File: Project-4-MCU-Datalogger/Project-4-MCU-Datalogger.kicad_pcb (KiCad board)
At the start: 2 copper layers, 0 parts

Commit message: update PCBNew from Schematic
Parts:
- added BT1: Battery, Connector_PinHeader_2.54mm:PinHeader_1x02_P2.54mm_Vertical, F.Cu at (208.3, 96.0)
- added C1: 0.1uF, Capacitor_SMD:C_0805_2012Metric, F.Cu at (230.6, 86.2)
- added C2: 22pF, Capacitor_SMD:C_0805_2012Metric, F.Cu at (230.6, 89.2)
- added C3: 22pF, Capacitor_SMD:C_0805_2012Metric, F.Cu at (230.6, 92.2)
- added C4: 0.1uF, Capacitor_SMD:C_0805_2012Metric, F.Cu at (230.6, 95.2)
- added C5: 100nF, Capacitor_SMD:C_0805_2012Metric, F.Cu at (230.6, 98.2)
- added D1: LED, LED_SMD:LED_0805_2012Metric, F.Cu at (235.1, 86.2)
- added D2: LED, LED_SMD:LED_0805_2012Metric, F.Cu at (235.1, 89.2)
- added H1: MountingHole, MountingHole:MountingHole_2.1mm, F.Cu at (208.9, 73.6)
- added H2: MountingHole, MountingHole:MountingHole_2.1mm, F.Cu at (208.9, 79.4)
- added H3: MountingHole, MountingHole:MountingHole_2.1mm, F.Cu at (208.9, 85.1)
- added H4: MountingHole, MountingHole:MountingHole_2.1mm, F.Cu at (208.9, 90.9)
- added J1: Conn_01x04_Pin, Connector_PinHeader_2.54mm:PinHeader_1x04_P2.54mm_Vertical, F.Cu at (246.2, 73.0)
- added J2: Conn_01x04_Pin, Connector_PinHeader_2.54mm:PinHeader_1x04_P2.54mm_Vertical, F.Cu at (250.8, 73.0)
- added J3: Conn_01x09_Pin, Connector_PinHeader_2.54mm:PinHeader_1x09_P2.54mm_Vertical, F.Cu at (241.6, 73.0)
- added J4: Conn_02x03_Odd_Even, Connector_PinHeader_2.54mm:PinHeader_2x03_P2.54mm_Vertical, F.Cu at (246.2, 85.3)
- added R1: 10K, Resistor_SMD:R_0805_2012Metric, F.Cu at (214.0, 72.2)
- added R2: 10K, Resistor_SMD:R_0805_2012Metric, F.Cu at (214.0, 75.2)
- added R3: 4.7K, Resistor_SMD:R_0805_2012Metric, F.Cu at (214.0, 78.1)
- added R4: 4.7K, Resistor_SMD:R_0805_2012Metric, F.Cu at (214.0, 81.1)
- added R5: 330, Resistor_SMD:R_0805_2012Metric, F.Cu at (214.0, 84.0)
- added R6: 10K, Resistor_SMD:R_0805_2012Metric, F.Cu at (214.0, 87.0)
- added R7: 330, Resistor_SMD:R_0805_2012Metric, F.Cu at (214.0, 89.9)
- added U1: 24LC1025, Package_SO:SOIC-8_5.3x5.3mm_P1.27mm, F.Cu at (221.3, 74.3)
- added U2: 24LC1025, Package_SO:SOIC-8_5.3x5.3mm_P1.27mm, F.Cu at (221.3, 81.2)
- added U3: DS1337S_, DS1337S_:SOIC127P600X175-8N, F.Cu at (221.3, 99.3)
- added U4: ATMEGA328P-AU, ATMEGA328P-AU:QFP80P900X900X120-32N, F.Cu at (222.7, 90.3)
- added Y1: 16 MHz, Crystal:Crystal_SMD_5032-2Pin_5.0x3.2mm_HandSoldering, F.Cu at (231.7, 73.4)
- added Y2: 32.768 KHz, Crystal:Crystal_SMD_5032-2Pin_5.0x3.2mm_HandSoldering, F.Cu at (231.7, 78.6)

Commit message: place footprints
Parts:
- moved J3 184.3 mm to (57.3, 77.8), turned to 90 degrees
- moved Y2 179.2 mm to (52.8, 69.0), turned to 90 degrees
- moved J2 167.9 mm to (82.9, 77.8), turned to 90 degrees
- moved C1 166.2 mm to (68.0, 52.0)
- moved C3 163.6 mm to (72.0, 52.0)
- moved U3 163.5 mm to (60.8, 68.2)
- moved U1 162.2 mm to (60.5, 53.5)
- moved U2 162.2 mm to (60.5, 60.5)
- moved C5 161.1 mm to (76.2, 52.2)
- moved BT1 160.0 mm to (52.8, 58.5)
- moved H1 157.8 mm to (52.5, 52.2)
- moved H3 156.5 mm to (52.5, 77.8)
- moved Y1 156.4 mm to (75.2, 71.8), turned to 180 degrees
- moved R1 156.0 mm to (58.0, 73.5)
- moved D2 154.1 mm to (85.2, 53.2)
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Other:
- board outline added: 50 x 30 mm

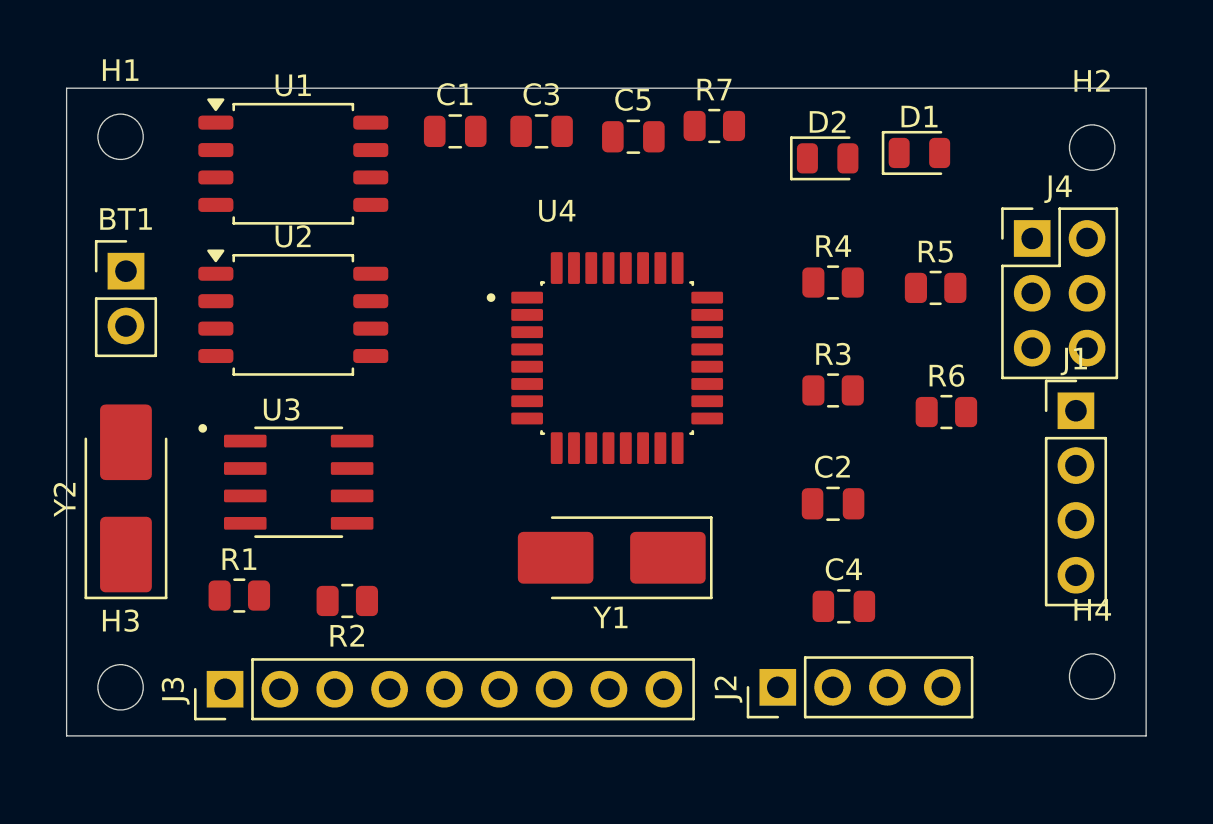
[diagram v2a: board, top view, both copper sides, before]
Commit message: wire signals, Vcc, GND, and add GND plane on back side
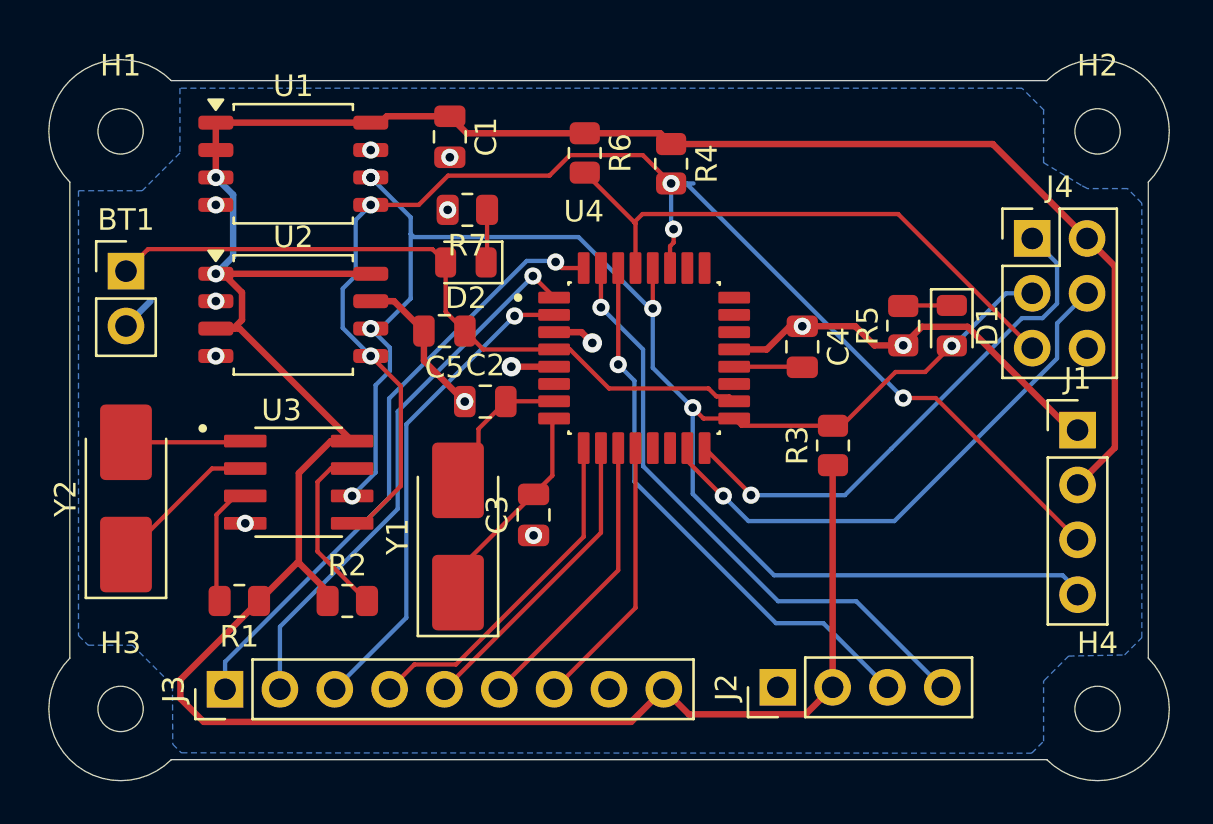
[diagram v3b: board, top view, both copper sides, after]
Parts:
- moved R6 20.6 mm to (74.0, 53.0), turned to -90 degrees
- moved C3 17.8 mm to (71.6, 69.8), turned to 90 degrees
- moved D2 17.4 mm to (68.5, 58.1), turned to 180 degrees
- moved C2 16.8 mm to (69.4, 64.5)
- moved C5 12.6 mm to (67.5, 61.2), turned to 180 degrees
- moved C4 12.2 mm to (84.1, 62.0), turned to -90 degrees
- moved R7 12.1 mm to (68.6, 55.6), turned to 180 degrees
- moved R4 9.30 mm to (78.0, 53.5), turned to -90 degrees
- moved D1 8.14 mm to (91.0, 61.0), turned to -90 degrees
- moved Y1 7.19 mm to (68.1, 70.8), turned to 90 degrees
- moved R3 2.55 mm to (85.5, 66.5), turned to 90 degrees
- moved R5 2.30 mm to (88.8, 61.0), turned to 90 degrees
- moved H4 1.52 mm to (97.8, 78.8)
- moved U4 1.25 mm to (76.8, 62.5)
- moved H3 1.00 mm to (52.5, 78.8)
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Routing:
- net /Vcc: track 0.00 -> 144.0 mm, vias 0 -> 2
- net /SCK: track 0.00 -> 80.0 mm, vias 0 -> 9
- net /SDA: track 0.00 -> 64.0 mm, vias 0 -> 5
- net Net-(BT1-+): track 0.00 -> 33.2 mm
- net GND: track 0.00 -> 31.8 mm, vias 0 -> 18
- net /D2: track 0.00 -> 28.4 mm, vias 0 -> 2
- net /TX: track 0.00 -> 28.1 mm, vias 0 -> 2
- net /RESET: track 0.00 -> 26.6 mm
- net /RX: track 0.00 -> 25.9 mm, vias 0 -> 2
- net /MOSI: track 0.00 -> 25.6 mm, vias 0 -> 3
- net /D3: track 0.00 -> 25.4 mm, vias 0 -> 2
- net /MISO: track 0.00 -> 24.4 mm, vias 0 -> 2
- net /D4: track 0.00 -> 22.6 mm, vias 0 -> 2
- net /D5: track 0.00 -> 16.0 mm
- net /D6: track 0.00 -> 14.2 mm
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- added copper zone on B.Cu, net GND
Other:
- board size 50 x 30 mm -> 51.9 x 33.4 mm

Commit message: re-arrange tracks and footprints, run DRC and fix DRC issues
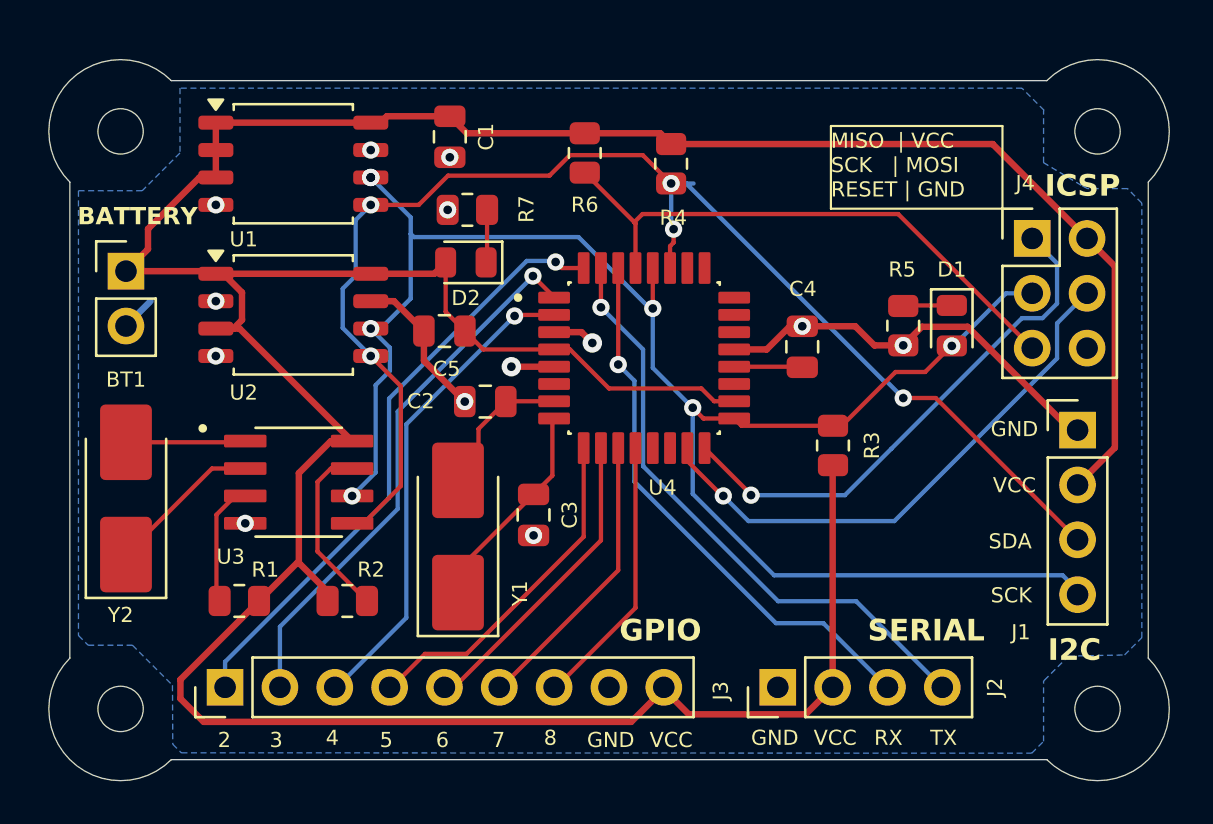
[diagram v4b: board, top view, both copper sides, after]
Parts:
- moved J3 0.09 mm to (57.3, 77.8)
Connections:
- BT1 pad 1: Net-(BT1-+) -> /Vcc
- C5 pad 1: Net-(BT1-+) -> /Vcc
- D2 pad 2: Net-(BT1-+) -> /Vcc
- U4 pad 18: Net-(BT1-+) -> /Vcc
- U4 pad 4: Net-(BT1-+) -> /Vcc
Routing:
- net Net-(BT1-+): track 33.2 -> 0.00 mm
- net /Vcc: track 144.0 -> 171.1 mm, vias 2 -> 0
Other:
- board text added: "2"
- board text added: "3"
- board text added: "4"
- board text added: "5"
- board text added: "6"
- board text added: "7"
- board text added: "8"
- board text added: "BATTERY"
- board text added: "GND"
- board text added: "GPIO"
- board text added: "I2C"
- board text added: "ICSP"
- board text added: "MISO | VCC SCK | MOSI RESET | GND"
- board text added: "RX"
- board text added: "SCK"
- board text added: "SDA"
- board text added: "SERIAL"
- board text added: "TX"
- board text added: "VCC"

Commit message: add text descriptions on front side, and silkscreen logo and descr. on back side
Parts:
- added REF**: KiCad-Logo2_5mm_SilkScreen, Symbol:KiCad-Logo2_5mm_SilkScreen, B.Cu at (86.2, 53.5)
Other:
- board text added: "+"
- board text added: "-"

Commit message: add technical details on the back silkscreen
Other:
- board text removed: "+"
- board text removed: "-"
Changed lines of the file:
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@@
+		)
+	)
+	(gr_text "VCC"
+		(at 55.5 59.3 90)
+		(layer "F.SilkS")
+		(effects
+			(font
+				(size 0.7 0.7)
+				(thickness 0.1)
+			)
+			(justify left bottom)
+		)
+	)
+	(gr_text "GND"
+		(at 55.5 62.4 90)
+		(layer "F.SilkS")
+		(effects
+			(font
+				(size 0.7 0.7)
+				(thickness 0.1)
+			)
+			(justify left bottom)
 		)
 	)
@@
 	(gr_text "BATTERY"
 		(at 50.5 56.4 0)
-		(layer "F.SilkS")
-		(effects
-			(font
-				(size 0.8 0.8)
-				(thickness 0.2)
-				(bold yes)
-			)
-			(justify left bottom)
-		)
-	)
-	(gr_text "+"
-		(at 54.4 57.4 0)
-		(layer "F.SilkS")
-		(effects
-			(font
-				(size 0.8 0.8)
-				(thickness 0.2)
-				(bold yes)
-			)
-			(justify left bottom)
-		)
-	)
-	(gr_text "-"
-		(at 54.4 63 0)
 		(layer "F.SilkS")
 		(effects
@@
 		)
 	)
-	(gr_text_box "Data logger with ATMega328P\nby jquk"
-		(start 56.399999 56.9)
-		(end 92.5 63.733041)
+	(gr_text_box "Data logger with ATMega328P,\nby jquk:\n- 2Mbit EEPROM\n- RTC\n- I2C, SPI, GPIOs"
+		(start 55.749999 56.9)
+		(end 92.5 70.977789)
 		(margins 1.0025 1.0025 1.0025 1.0025)
 		(layer "B.SilkS")
